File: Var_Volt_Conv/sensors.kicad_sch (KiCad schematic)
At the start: 8 parts, among them U401 INA215BIDCKR, U402 INA215BIDCKR

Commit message: Added footprints to all components except the connectors and buck-boost converter
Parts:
- R401, R402: footprint (none) -> Resistor_SMD:R_0603_1608Metric
- R403, R404: footprint (none) -> Resistor_SMD:R_0402_1005Metric
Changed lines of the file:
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@@
 			)
 		)
-		(property "Footprint" ""
+		(property "Footprint" "Resistor_SMD:R_0402_1005Metric"
 			(at 85.852 129.54 90)
 			(effects
@@
 			)
 		)
-		(property "Footprint" ""
+		(property "Footprint" "Resistor_SMD:R_0603_1608Metric"
 			(at 87.122 57.15 90)
 			(effects
@@
 			)
 		)
-		(property "Footprint" ""
+		(property "Footprint" "Resistor_SMD:R_0402_1005Metric"
 			(at 85.852 144.78 90)
 			(effects
@@
 			)
 		)
-		(property "Footprint" ""
+		(property "Footprint" "Resistor_SMD:R_0603_1608Metric"
 			(at 87.122 72.39 90)
 			(effects

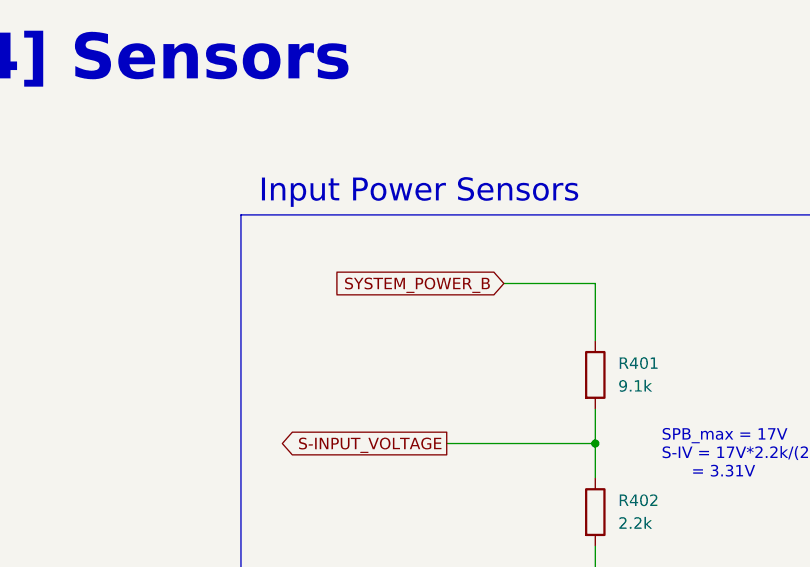
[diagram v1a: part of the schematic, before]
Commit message: Finish organizing sub-circuits, and input voltage sensor sensing System_voltage_input_A instead of B
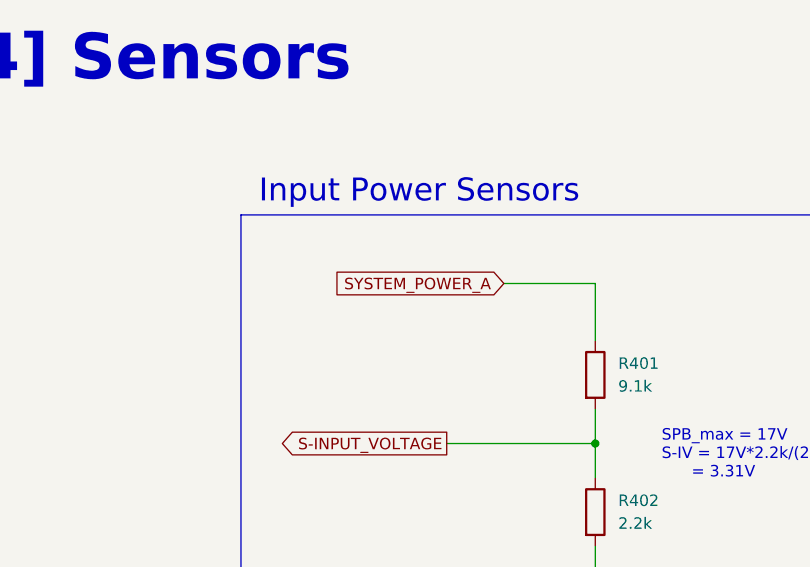
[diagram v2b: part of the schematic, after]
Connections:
- net SYSTEM_POWER_A: now also R401.1
- net SYSTEM_POWER_B: no longer R401.1
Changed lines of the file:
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@@
 		)
 	)
-	(global_label "SYSTEM_POWER_B"
+	(global_label "SYSTEM_POWER_A"
 		(shape input)
 		(at 78.74 46.99 180)
@@
 		)
 		(property "Intersheetrefs" "${INTERSHEET_REFS}"
-			(at 59.0031 46.99 0)
+			(at 59.1845 46.99 0)
 			(effects
 				(font

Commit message: Add Power, digital and analog grounds
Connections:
- net GND renamed GNDA
- net GNDA: no longer R402.2, R404.2
- new net GNDPWR: R402.2, R404.2

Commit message: Labeled subcircuits in PCB
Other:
- title: (none) -> Variable Voltage Controller
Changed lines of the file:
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@@
 	(generator_version "8.0")
 	(paper "A4")
+	(title_block
+		(title "Variable Voltage Controller")
+		(date "2025-02-02")
+		(rev "1.0")
+	)
 	(junction
 		(at 189.23 78.74)

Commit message: Change difference amplifieres in sensor section form 75V/V to 50V/V
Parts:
- U401, U402: value INA215BIDCKR -> INA213AIDCKR
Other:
- note added: "INA213AIDCKR are current-sense amps with a gain of 50V/V"
- note added: "Imax = 6A Gain = 50V/V Rsense = 11mohm 3.3V = Imax*Gain*Rsense"
- note removed: "INA215BIDCKR are current-sense amps with a gain of 75V/V"
- note removed: "Imax = 4A Gain = 75V/V Rsense = 11mohm 3.3V = Imax*Gain*Rsense"
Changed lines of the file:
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@@
 		)
 	)
-	(text "INA215BIDCKR are current-sense amps\nwith a gain of 75V/V"
+	(text "INA213AIDCKR are current-sense amps\nwith a gain of 50V/V"
 		(exclude_from_sim no)
 		(at 202.692 68.326 0)
@@
 		)
 	)
-	(text "Imax = 4A\nGain = 75V/V\nRsense = 11mohm\n3.3V = Imax*Gain*Rsense"
+	(text "Imax = 6A\nGain = 50V/V\nRsense = 11mohm\n3.3V = Imax*Gain*Rsense"
 		(exclude_from_sim no)
 		(at 220.218 146.558 0)
@@
 			)
 		)
-		(property "Value" "INA215BIDCKR"
+		(property "Value" "INA213AIDCKR"
 			(at 188.468 127 0)
 			(effects
@@
 			)
 		)
-		(property "Description" "Current Sense Amplifier 1 Circuit Single-Ended SC-70-6, Gain 75V/V"
+		(property "Description" "Current Sense Amplifier 1 Circuit Single-Ended SC-70-6, Gain 50V/V"
 			(at 203.708 160.02 0)
 			(effects
@@
 			)
 		)
-		(property "Value" "INA215BIDCKR"
+		(property "Value" "INA213AIDCKR"
 			(at 174.498 53.34 0)
 			(effects
@@
 			)
 		)
-		(property "Description" "Current Sense Amplifier 1 Circuit Single-Ended SC-70-6, Gain 75V/V"
+		(property "Description" "Current Sense Amplifier 1 Circuit Single-Ended SC-70-6, Gain 50V/V"
 			(at 189.738 86.36 0)
 			(effects

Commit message: Completed the BOM
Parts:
- C401, C402: JLCPCB Part # (none) -> C155422; Manufacturer Part # (none) -> CL05B104KA5NNNC
- R401: JLCPCB Part # (none) -> C114639; Manufacturer Part # (none) -> RC0603FR-079K1L
- R402: JLCPCB Part # (none) -> C114662; Manufacturer Part # (none) -> RC0603FR-072K2L
- R403: JLCPCB Part # (none) -> C409902; Manufacturer Part # (none) -> ERJ2RKF2402X
- R404: JLCPCB Part # (none) -> C400631; Manufacturer Part # (none) -> ERJ2RKF4701X
- U401, U402: JLCPCB Part # (none) -> C129346; Manufacturer Part # (none) -> INA213AIDCKR
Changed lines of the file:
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@@
+			)
+		)
+		(property "JLCPCB Part #" "C129346"
+			(at 203.2 138.43 0)
+			(effects
+				(font
+					(size 1.27 1.27)
+				)
+				(hide yes)
+			)
+		)
+		(property "Manufacturer Part #" "INA213AIDCKR"
+			(at 203.2 138.43 0)
+			(effects
+				(font
+					(size 1.27 1.27)
+				)
+				(hide yes)
 			)
 		)
@@
 			)
 		)
+		(property "JLCPCB Part #" "C155422"
+			(at 204.47 48.26 0)
+			(effects
+				(font
+					(size 1.27 1.27)
+				)
+				(hide yes)
+			)
+		)
+		(property "Manufacturer Part #" "CL05B104KA5NNNC"
+			(at 204.47 48.26 0)
+			(effects
+				(font
+					(size 1.27 1.27)
+				)
+				(hide yes)
+			)
+		)
 		(pin "1"
 		)
@@
 			)
 		)
+		(property "JLCPCB Part #" "C409902"
+			(at 87.63 129.54 0)
+			(effects
+				(font
+					(size 1.27 1.27)
+				)
+				(hide yes)
+			)
+		)
+		(property "Manufacturer Part #" "ERJ2RKF2402X"
+			(at 87.63 129.54 0)
+			(effects
+				(font
+					(size 1.27 1.27)
+				)
+				(hide yes)
+			)
+		)
 		(pin "2"
 		)
@@
 			)
 		)
+		(property "JLCPCB Part #" "C114639"
+			(at 88.9 57.15 0)
+			(effects
+				(font
+					(size 1.27 1.27)
+				)
+				(hide yes)
+			)
+		)
+		(property "Manufacturer Part #" "RC0603FR-079K1L"
+			(at 88.9 57.15 0)
+			(effects
+				(font
+					(size 1.27 1.27)
+				)
+				(hide yes)
+			)
+		)
 		(pin "2"
 		)
@@
 			)
 		)
+		(property "JLCPCB Part #" "C155422"
+			(at 218.44 120.65 0)
+			(effects
+				(font
+					(size 1.27 1.27)
+				)
+				(hide yes)
+			)
+		)
+		(property "Manufacturer Part #" "CL05B104KA5NNNC"
+			(at 218.44 120.65 0)
+			(effects
+				(font
+					(size 1.27 1.27)
+				)
+				(hide yes)
+			)
+		)
 		(pin "1"
 		)
@@
 			)
 		)
+		(property "JLCPCB Part #" "C400631"
+			(at 87.63 144.78 0)
+			(effects
+				(font
+					(size 1.27 1.27)
+				)
+				(hide yes)
+			)
+		)
+		(property "Manufacturer Part #" "ERJ2RKF4701X"
+			(at 87.63 144.78 0)
+			(effects
+				(font
+					(size 1.27 1.27)
+				)
+				(hide yes)
+			)
+		)
 		(pin "2"
 		)
@@
 			)
 		)
+		(property "JLCPCB Part #" "C114662"
+			(at 88.9 72.39 0)
+			(effects
+				(font
+					(size 1.27 1.27)
+				)
+				(hide yes)
+			)
+		)
+		(property "Manufacturer Part #" "RC0603FR-072K2L"
+			(at 88.9 72.39 0)
+			(effects
+				(font
+					(size 1.27 1.27)
+				)
+				(hide yes)
+			)
+		)
 		(pin "2"
 		)
@@
 			(effects
 				(font
+					(size 1.27 1.27)
+				)
+				(hide yes)
+			)
+		)
+		(property "JLCPCB Part #" "C129346"
+			(at 189.23 64.77 0)
+			(effects
+				(font
+					(size 1.27 1.27)
+				)
+				(hide yes)
+			)
+		)
+		(property "Manufacturer Part #" "INA213AIDCKR"
+			(at 189.23 64.77 0)
+			(effects
+				(font

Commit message: Updated schematic, C121, R112 and SW201 now use components that are still in stock on JLCPCB
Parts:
- C401, C402: JLCPCB Part # C155422 -> (none); LCSC (none) -> C155422
- R401: JLCPCB Part # C114639 -> (none); LCSC (none) -> C114639
- R402: JLCPCB Part # C114662 -> (none); LCSC (none) -> C114662
- R403: JLCPCB Part # C409902 -> (none); LCSC (none) -> C409902
- R404: JLCPCB Part # C400631 -> (none); LCSC (none) -> C400631
- U401, U402: JLCPCB Part # C129346 -> (none); LCSC (none) -> C129346
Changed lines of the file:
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@@
 			)
 		)
-		(property "JLCPCB Part #" "C129346"
+		(property "Manufacturer Part #" "INA213AIDCKR"
 			(at 203.2 138.43 0)
 			(effects
@@
 			)
 		)
-		(property "Manufacturer Part #" "INA213AIDCKR"
+		(property "LCSC" "C129346"
 			(at 203.2 138.43 0)
 			(effects
@@
 			)
 		)
-		(property "JLCPCB Part #" "C155422"
+		(property "Manufacturer Part #" "CL05B104KA5NNNC"
 			(at 204.47 48.26 0)
 			(effects
@@
 			)
 		)
-		(property "Manufacturer Part #" "CL05B104KA5NNNC"
+		(property "LCSC" "C155422"
 			(at 204.47 48.26 0)
 			(effects
@@
 			)
 		)
-		(property "JLCPCB Part #" "C409902"
+		(property "Manufacturer Part #" "ERJ2RKF2402X"
 			(at 87.63 129.54 0)
 			(effects
@@
 			)
 		)
-		(property "Manufacturer Part #" "ERJ2RKF2402X"
+		(property "LCSC" "C409902"
 			(at 87.63 129.54 0)
 			(effects
@@
 			)
 		)
-		(property "JLCPCB Part #" "C114639"
+		(property "Manufacturer Part #" "RC0603FR-079K1L"
 			(at 88.9 57.15 0)
 			(effects
@@
 			)
 		)
-		(property "Manufacturer Part #" "RC0603FR-079K1L"
+		(property "LCSC" "C114639"
 			(at 88.9 57.15 0)
 			(effects
@@
 			)
 		)
-		(property "JLCPCB Part #" "C155422"
+		(property "Manufacturer Part #" "CL05B104KA5NNNC"
 			(at 218.44 120.65 0)
 			(effects
@@
 			)
 		)
-		(property "Manufacturer Part #" "CL05B104KA5NNNC"
+		(property "LCSC" "C155422"
 			(at 218.44 120.65 0)
 			(effects
@@
 			)
 		)
-		(property "JLCPCB Part #" "C400631"
+		(property "Manufacturer Part #" "ERJ2RKF4701X"
 			(at 87.63 144.78 0)
 			(effects
@@
 			)
 		)
-		(property "Manufacturer Part #" "ERJ2RKF4701X"
+		(property "LCSC" "C400631"
 			(at 87.63 144.78 0)
 			(effects
@@
 			)
 		)
-		(property "JLCPCB Part #" "C114662"
+		(property "Manufacturer Part #" "RC0603FR-072K2L"
 			(at 88.9 72.39 0)
 			(effects
@@
 			)
 		)
-		(property "Manufacturer Part #" "RC0603FR-072K2L"
+		(property "LCSC" "C114662"
 			(at 88.9 72.39 0)
 			(effects
@@
 			)
 		)
-		(property "JLCPCB Part #" "C129346"
-			(at 189.23 64.77 0)
-			(effects
-				(font
-					(size 1.27 1.27)
-				)
-				(hide yes)
-			)
-		)
 		(property "Manufacturer Part #" "INA213AIDCKR"
 			(at 189.23 64.77 0)
 			(effects
+				(font
+					(size 1.27 1.27)
+				)
+				(hide yes)
+			)
+		)
+		(property "LCSC" "C129346"
+			(at 189.23 64.77 0)
+			(effects

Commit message: Confirmed all basic components
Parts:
- C401, C402: LCSC C155422 -> (none); lcsc (none) -> C155422
- R401: LCSC C114639 -> (none); Manufacturer Part # RC0603FR-079K1L -> 0603WAF9101T5E; lcsc (none) -> C23260
- R402: LCSC C114662 -> (none); Manufacturer Part # RC0603FR-072K2L -> 0603WAF2201T5E; lcsc (none) -> C4190
- R403: LCSC C409902 -> (none); lcsc (none) -> C409902
- R404: value 4.7K -> 4.75K; LCSC C400631 -> (none); Manufacturer Part # ERJ2RKF4701X -> 0402WGF4751TCE; lcsc (none) -> C25901
- U401, U402: LCSC C129346 -> (none); lcsc (none) -> C129346
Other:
- note added: "SPB_max = 20V S-IV = 20V*4.75k/(4.75k + 24k) = 3.30V"
- note removed: "SPB_max = 20V S-IV = 17V*4.7k/(4.7k + 24k) = 3.27V"
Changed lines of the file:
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@@
 		)
 	)
-	(text "SPB_max = 20V\nS-IV = 17V*4.7k/(4.7k + 24k)\n      = 3.27V"
+	(text "SPB_max = 20V\nS-IV = 20V*4.75k/(4.75k + 24k)\n      = 3.30V"
 		(exclude_from_sim no)
 		(at 96.266 139.7 0)
@@
 			)
 		)
-		(property "LCSC" "C129346"
+		(property "lcsc" "C129346"
 			(at 203.2 138.43 0)
 			(effects
@@
 			)
 		)
-		(property "LCSC" "C155422"
+		(property "lcsc" "C155422"
 			(at 204.47 48.26 0)
 			(effects
@@
 			)
 		)
-		(property "LCSC" "C409902"
+		(property "lcsc" "C409902"
 			(at 87.63 129.54 0)
 			(effects
@@
 			)
 		)
-		(property "Manufacturer Part #" "RC0603FR-079K1L"
+		(property "Manufacturer Part #" "0603WAF9101T5E"
 			(at 88.9 57.15 0)
 			(effects
@@
 			)
 		)
-		(property "LCSC" "C114639"
+		(property "lcsc" "C23260"
 			(at 88.9 57.15 0)
 			(effects
@@
 			)
 		)
-		(property "LCSC" "C155422"
+		(property "lcsc" "C155422"
 			(at 218.44 120.65 0)
 			(effects
@@
 			)
 		)
-		(property "Value" "4.7K"
+		(property "Value" "4.75K"
 			(at 90.17 146.0499 0)
 			(effects
@@
 			)
 		)
-		(property "Manufacturer Part #" "ERJ2RKF4701X"
+		(property "Manufacturer Part #" "0402WGF4751TCE"
 			(at 87.63 144.78 0)
 			(effects
@@
 			)
 		)
-		(property "LCSC" "C400631"
+		(property "lcsc" "C25901 "
 			(at 87.63 144.78 0)
 			(effects
@@
 			)
 		)
-		(property "Manufacturer Part #" "RC0603FR-072K2L"
+		(property "Manufacturer Part #" "0603WAF2201T5E"
 			(at 88.9 72.39 0)
 			(effects
@@
 			)
 		)
-		(property "LCSC" "C114662"
+		(property "lcsc" "C4190"
 			(at 88.9 72.39 0)
 			(effects
@@
 			)
 		)
-		(property "LCSC" "C129346"
+		(property "lcsc" "C129346"
 			(at 189.23 64.77 0)
 			(effects
